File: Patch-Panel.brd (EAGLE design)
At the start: 84.9 x 142.3 mm, 51 parts, among them J1 APPPP45_PCB_VERT, J10 APPPP45_PCB_VERT, J11 APPPP45_PCB_VERT, J12 APPPP45_PCB_VERT, J13 APPPP45_PCB_VERT, J14 APPPP45_PCB_VERT, J15 APPPP45_PCB_VERT, J16 APPPP45_PCB_VERT, J17 APPPP45_PCB_VERT, J18 APPPP45_PCB_VERT, J19 APPPP45_PCB_VERT, J2 APPPP45_PCB_VERT, J20 APPPP45_PCB_VERT, J21 APPPP45_PCB_VERT, J22 APPPP45_PCB_VERT, J23 APPPP45_PCB_VERT, J24 APPPP45_PCB_VERT, J25 APPPP45_PCB_VERT, J26 APPPP45_PCB_VERT, J27 APPPP45_PCB_VERT, J28 APPPP45_PCB_VERT, J29 APPPP45_PCB_VERT, J3 APPPP45_PCB_VERT, J30 APPPP45_PCB_VERT, J31 APPPP45_PCB_VERT, J32 APPPP45_PCB_VERT, J33 APPPP45_PCB_VERT, J34 APPPP45_PCB_VERT, J35 APPPP45_PCB_VERT, J36 APPPP45_PCB_VERT, J37 APPPP45_PCB_VERT, J38 APPPP45_PCB_VERT, J39 APPPP45_PCB_VERT, J4 APPPP45_PCB_VERT, J40 APPPP45_PCB_VERT, J41 APPPP45_PCB_VERT, J42 APPPP45_PCB_VERT, J43 APPPP45_PCB_VERT, J5 APPPP45_PCB_VERT, J6 APPPP45_PCB_VERT, J7 APPPP45_PCB_VERT, J8 APPPP45_PCB_VERT, J9 APPPP45_PCB_VERT

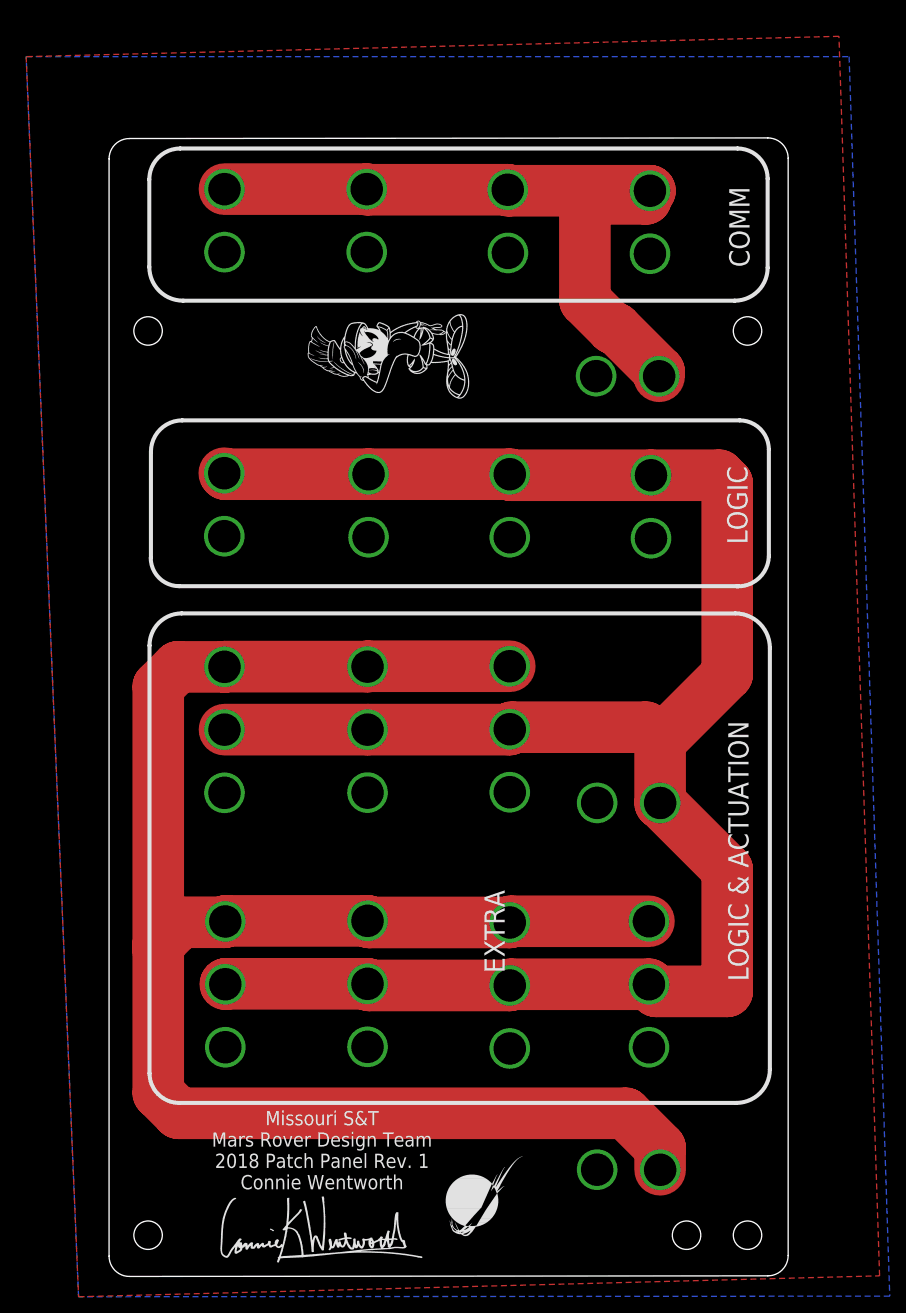
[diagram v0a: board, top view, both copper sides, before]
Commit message: Patch Panel Rev 2
Eliminates all exclusive logic buses and added seven more actuation/logic combo buses. Added one more comm bus
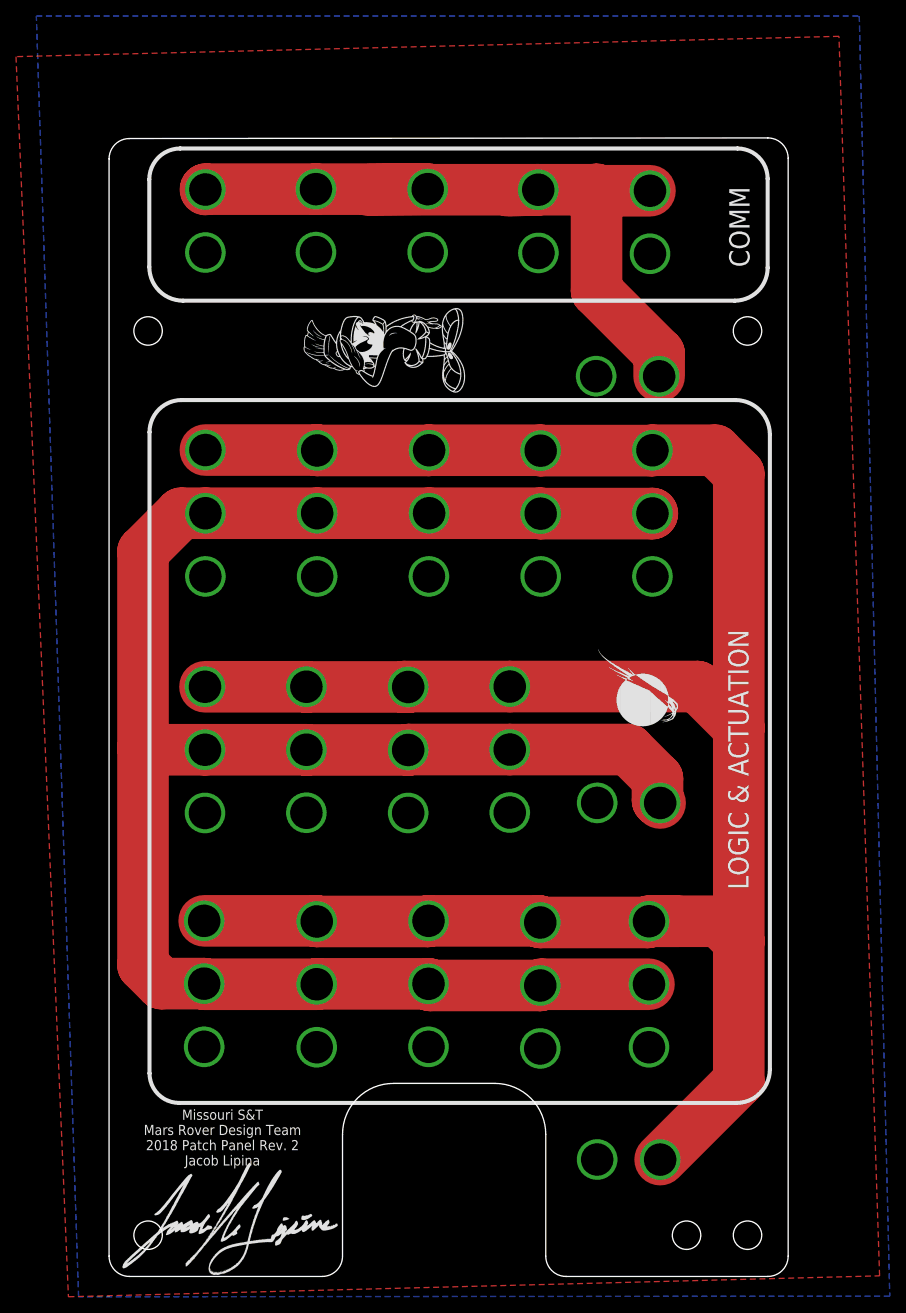
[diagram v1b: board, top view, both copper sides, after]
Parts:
- added J44, J45, J46, J47, J48, J49, J50, J51, J52, J53, J54, J55, J56, J57, J58: APPPP45_PCB_VERT, MRDT-Connectors:APP45_PCB_VERT
- U$1: value CONNIE_WENTWORTH_SIGNATURE -> JACOB_SIG; device MRDT-Signatures:CONNIE_WENTWORTH_SIGNATURE -> Jacob Signature:JACOB_SIG
- moved LOGO1 71.2 mm to (72.0, 68.8), turned to 90 degrees
- moved J41 54.9 mm to (21.5, 77.6)
- moved J13 42.8 mm to (21.5, 61.9)
- moved J39 40.3 mm to (64.8, 91.4)
- moved J40 35.3 mm to (21.5, 69.8)
- moved J25 34.7 mm to (8.84, 61.9)
- moved J43 33.5 mm to (8.84, 69.8)
- moved J42 32.7 mm to (64.5, 131.8)
- moved J27 31.9 mm to (8.74, 48.4)
- moved J16 31.9 mm to (8.74, 32.6)
- moved J23 31.9 mm to (8.74, 40.5)
- moved J36 17.4 mm to (22.9, 91.4)
- moved U$1 13.3 mm to (0.00, -2.54)
- moved J17 11.4 mm to (22.8, 40.5)
- moved J18 11.4 mm to (22.8, 48.3)
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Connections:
- net ACT-12V: now also J38.P$1, J41.P$1, J46.P$1, J49.P$1, J52.P$1, J55.P$1, J58.P$1
- net COM-12V: now also J44.P$1
- net GND: now also J36.P$1, J42.P$1, J45.P$1, J47.P$1, J50.P$1, J53.P$1, J56.P$1; no longer J37.P$1, J41.P$1, J43.P$1
- net LOG-12V: now also J37.P$1, J43.P$1, J48.P$1, J51.P$1, J54.P$1, J57.P$1; no longer J36.P$1, J38.P$1, J42.P$1
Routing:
- net ACT-12V: track 226.8 -> 299.6 mm
- net COM-12V: track 88.4 -> 101.1 mm
- net LOG-12V: track 252.5 -> 250.9 mm
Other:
- outline, holes or cut-outs redrawn
- board text added: "Missouri S&T Mars Rover Design Team 2018 Patch Panel Rev. 2 Jacob Lipina"
- board text removed: "EXTRA"
- board text removed: "Missouri S&T Mars Rover Design Team 2018 Patch Panel Rev. 1 Connie Wentworth"

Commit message: Rev.3 to Change Mounting Hole Locations
Mounting holes on Rev.2 are incorrect because power board's size changed slightly and we only realized the holes didnt match up after we ordered Rev.2
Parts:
- moved U$1 112.6 mm to (29.3, 106.2)
- moved U$2 103.2 mm to (27.8, 7.80)
- moved H3 5.08 mm to (9.98, 118.1)
- moved H6 5.08 mm to (9.98, 5.08)
- moved H4 0.08 mm to (79.8, 5.08)
- moved H5 0.08 mm to (72.2, 5.08)
- moved H7 0.08 mm to (79.8, 118.1)
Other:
- outline, holes or cut-outs redrawn
- board text added: "Missouri S&T Mars Rover 2018 Patch Panel Rev. 3 Jacob Lipina"
- board text removed: "Missouri S&T Mars Rover Design Team 2018 Patch Panel Rev. 2 Jacob Lipina"
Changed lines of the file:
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@@
 <setting verticaltext="up"/>
 </settings>
-<grid distance="0.05" unitdist="inch" unit="inch" style="lines" multiple="1" display="yes" altdistance="0.001" altunitdist="inch" altunit="inch"/>
+<grid distance="10" unitdist="mil" unit="mil" style="lines" multiple="1" display="yes" altdistance="5" altunitdist="mil" altunit="mil"/>
 <layers>
 <layer number="1" name="Top" color="4" fill="1" visible="yes" active="yes"/>
@@
 <layer number="45" name="Holes" color="7" fill="1" visible="no" active="yes"/>
 <layer number="46" name="Milling" color="3" fill="1" visible="no" active="yes"/>
-<layer number="47" name="Measures" color="7" fill="1" visible="no" active="yes"/>
+<layer number="47" name="Measures" color="7" fill="1" visible="yes" active="yes"/>
 <layer number="48" name="Document" color="7" fill="1" visible="yes" active="yes"/>
 <layer number="49" name="Reference" color="7" fill="1" visible="yes" active="yes"/>
@@
 <wire x1="82.3722" y1="142.3162" x2="2.5654" y2="142.24" width="0" layer="20"/>
 <wire x1="2.5654" y1="142.24" x2="0.0254" y2="139.7" width="0" layer="20" curve="90"/>
-<wire x1="0.0254" y1="139.7" x2="0.0254" y2="2.54" width="0" layer="20"/>
-<wire x1="0.0254" y1="2.54" x2="2.5654" y2="0" width="0" layer="20" curve="90"/>
+<wire x1="5.5372" y1="2.54" x2="5.5372" y2="21.59" width="0" layer="20"/>
+<wire x1="5.5372" y1="21.59" x2="2.9972" y2="24.13" width="0" layer="20" curve="90"/>
+<wire x1="2.9972" y1="24.13" x2="2.5654" y2="24.13" width="0" layer="20"/>
+<wire x1="2.5654" y1="24.13" x2="0.0254" y2="26.67" width="0" layer="20" curve="-90"/>
+<wire x1="0.0254" y1="26.67" x2="0.0254" y2="139.7" width="0" layer="20"/>
 <text x="74.8538" y="109.7788" size="1.778" layer="26" font="vector" rot="MR90">COMM</text>
 <text x="74.8792" y="55.6768" size="1.778" layer="26" font="vector" rot="MR90">LOGIC</text>
@@
 <text x="77.5462" y="136.2202" size="2.54" layer="21" font="vector" rot="R270">COMM</text>
 <text x="79.9592" y="48.3362" size="2.54" layer="21" font="vector" rot="R90">LOGIC &amp; ACTUATION</text>
-<text x="14.1986" y="13.8684" size="1.27" layer="21" font="vector" align="bottom-center">Missouri S&amp;T
-Mars Rover Design Team
-2018 Patch Panel Rev. 2
-Jacob Lipina</text>
+<text x="21.0566" y="112.1918" size="1.4224" layer="21" font="vector" align="bottom-center">      Missouri S&amp;T
+  Mars Rover 2018
+Patch Panel Rev. 3
+     Jacob Lipina</text>
 <wire x1="78.4352" y1="21.6916" x2="8.7884" y2="21.6916" width="0.508" layer="21"/>
 <wire x1="8.7884" y1="21.6916" x2="5.08" y2="25.4" width="0.508" layer="21" curve="-90"/>
@@
 <wire x1="29.21" y1="17.78" x2="29.21" y2="2.54" width="0" layer="20"/>
 <wire x1="29.21" y1="2.54" x2="26.67" y2="0" width="0" layer="20" curve="-90"/>
-<wire x1="26.67" y1="0" x2="2.54" y2="0" width="0" layer="20"/>
+<wire x1="26.67" y1="0" x2="8.0772" y2="0" width="0" layer="20"/>
+<wire x1="8.0772" y1="0" x2="5.5372" y2="2.54" width="0" layer="20" curve="-90"/>
+<dimension x1="79.8322" y1="5.08" x2="79.8068" y2="0" x3="98.044" y3="2.54" textsize="1.778" layer="47" dtype="vertical" unit="mil"/>
+<dimension x1="72.2122" y1="5.08" x2="72.6186" y2="0" x3="101.1936" y3="2.54" textsize="1.778" layer="47" dtype="vertical" unit="mil"/>
+<dimension x1="9.9822" y1="5.08" x2="10.0076" y2="0" x3="-2.1082" y3="2.54" textsize="1.778" layer="47" dtype="vertical" unit="mil"/>
+<dimension x1="9.9822" y1="118.11" x2="10.0076" y2="0" x3="-6.1722" y3="59.055" textsize="1.778" layer="47" dtype="vertical" unit="mil"/>
+<dimension x1="82.3722" y1="0" x2="79.8322" y2="118.11" x3="104.0384" y3="59.055" textsize="1.778" layer="47" dtype="vertical" unit="mil"/>
+<dimension x1="84.9122" y1="2.54" x2="79.8322" y2="5.08" x3="82.3722" y3="-2.8956" textsize="1.778" layer="47" dtype="horizontal" unit="mil"/>
+<dimension x1="84.9122" y1="2.54" x2="72.2122" y2="5.08" x3="78.5622" y3="-7.4168" textsize="1.778" layer="47" dtype="horizontal" unit="mil"/>
+<dimension x1="84.9122" y1="2.54" x2="9.9822" y2="5.08" x3="47.4472" y3="-11.5062" textsize="1.778" layer="47" dtype="horizontal" unit="mil"/>
+<dimension x1="9.9822" y1="118.11" x2="84.9122" y2="116.205" x3="47.4472" y3="147.7264" textsize="1.778" layer="47" dtype="horizontal" unit="mil"/>
+<dimension x1="84.9122" y1="2.54" x2="54.61" y2="4.2164" x3="69.7611" y3="-14.986" textsize="1.778" layer="47" dtype="horizontal" unit="mil"/>
+<dimension x1="84.9122" y1="2.54" x2="29.21" y2="3.6068" x3="57.0611" y3="-20.4978" textsize="1.778" layer="47" dtype="horizontal" unit="mil"/>
+<dimension x1="35.56" y1="24.13" x2="16.7894" y2="0" x3="-8.763" y3="12.065" textsize="1.778" layer="47" dtype="vertical" unit="mil"/>
+<wire x1="32.258" y1="120.142" x2="32.258" y2="112.014" width="0.254" layer="21"/>
 </plain>
 <attributes>
@@
 <attribute name="COLOR1" value="" x="57.0992" y="62.3697" size="1.778" layer="28" rot="MR180" display="off"/>
 </element>
-<element name="H3" library="MRDT-Hardware" package="#6_SCREW" value="MOUNTING_HOLE#6" x="4.9022" y="118.1862"/>
-<element name="H4" library="MRDT-Hardware" package="#6_SCREW" value="MOUNTING_HOLE#6" x="79.8322" y="5.1562"/>
-<element name="H5" library="MRDT-Hardware" package="#6_SCREW" value="MOUNTING_HOLE#6" x="72.2122" y="5.1562"/>
-<element name="H6" library="MRDT-Hardware" package="#6_SCREW" value="MOUNTING_HOLE#6" x="4.9022" y="5.1562"/>
-<element name="H7" library="MRDT-Hardware" package="#6_SCREW" value="MOUNTING_HOLE#6" x="79.8322" y="118.1862"/>
+<element name="H3" library="MRDT-Hardware" package="#6_SCREW" value="MOUNTING_HOLE#6" x="9.9822" y="118.11"/>
+<element name="H4" library="MRDT-Hardware" package="#6_SCREW" value="MOUNTING_HOLE#6" x="79.8322" y="5.08"/>
+<element name="H5" library="MRDT-Hardware" package="#6_SCREW" value="MOUNTING_HOLE#6" x="72.2122" y="5.08"/>
+<element name="H6" library="MRDT-Hardware" package="#6_SCREW" value="MOUNTING_HOLE#6" x="9.9822" y="5.08"/>
+<element name="H7" library="MRDT-Hardware" package="#6_SCREW" value="MOUNTING_HOLE#6" x="79.8322" y="118.11"/>
 <element name="LOGO1" library="MRDT-Hardware" package="MRDT_LOGO" value="MRDT_LOGO" x="72.009" y="68.7578" rot="R90"/>
-<element name="U$2" library="MRDT-Hardware" package="MARVIN" value="MARVIN-THE-MARTIAN" x="45.0088" y="109.5502" rot="R90"/>
+<element name="U$2" library="MRDT-Hardware" package="MARVIN" value="MARVIN-THE-MARTIAN" x="27.8384" y="7.7978" rot="R90"/>
 <element name="J7" library="MRDT-Connectors" package="APP45_PCB_VERT" value="APPPP45_PCB_VERT" x="64.3382" y="32.5882" rot="R270">
 <attribute name="COLOR1" value="" x="64.3382" y="32.5882" size="1.778" layer="27" rot="R270" display="off"/>
@@
 <attribute name="COLOR1" value="" x="-753.1608" y="77.6478" size="1.778" layer="27" rot="R270" display="off"/>
 </element>
-<element name="U$1" library="Jacob Signature" package="JACOB_SIG" value="JACOB_SIG" x="0" y="-2.54"/>
+<element name="U$1" library="Jacob Signature" package="JACOB_SIG" value="JACOB_SIG" x="29.3116" y="106.1974"/>
 </elements>
 <signals>
